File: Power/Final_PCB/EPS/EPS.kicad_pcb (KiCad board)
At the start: 4 copper layers, 85 x 85 mm, 37 parts, among them J1 Left_Header, J2 Right_Header, U1 INA226, U2 MT3608-28, U3 LM2596S-5, U4 LM2596S-3.3

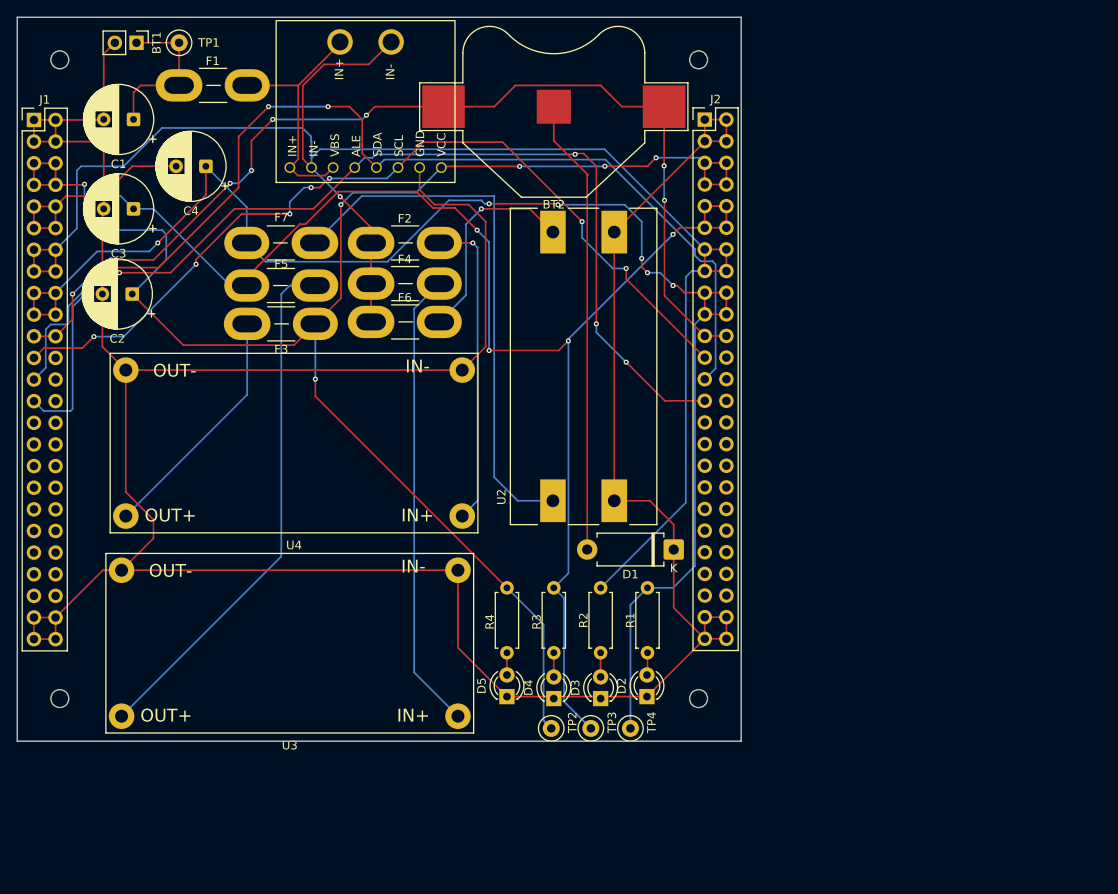
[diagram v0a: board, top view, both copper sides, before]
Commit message: Fixed EPS board to have 12V instead of 28V rail
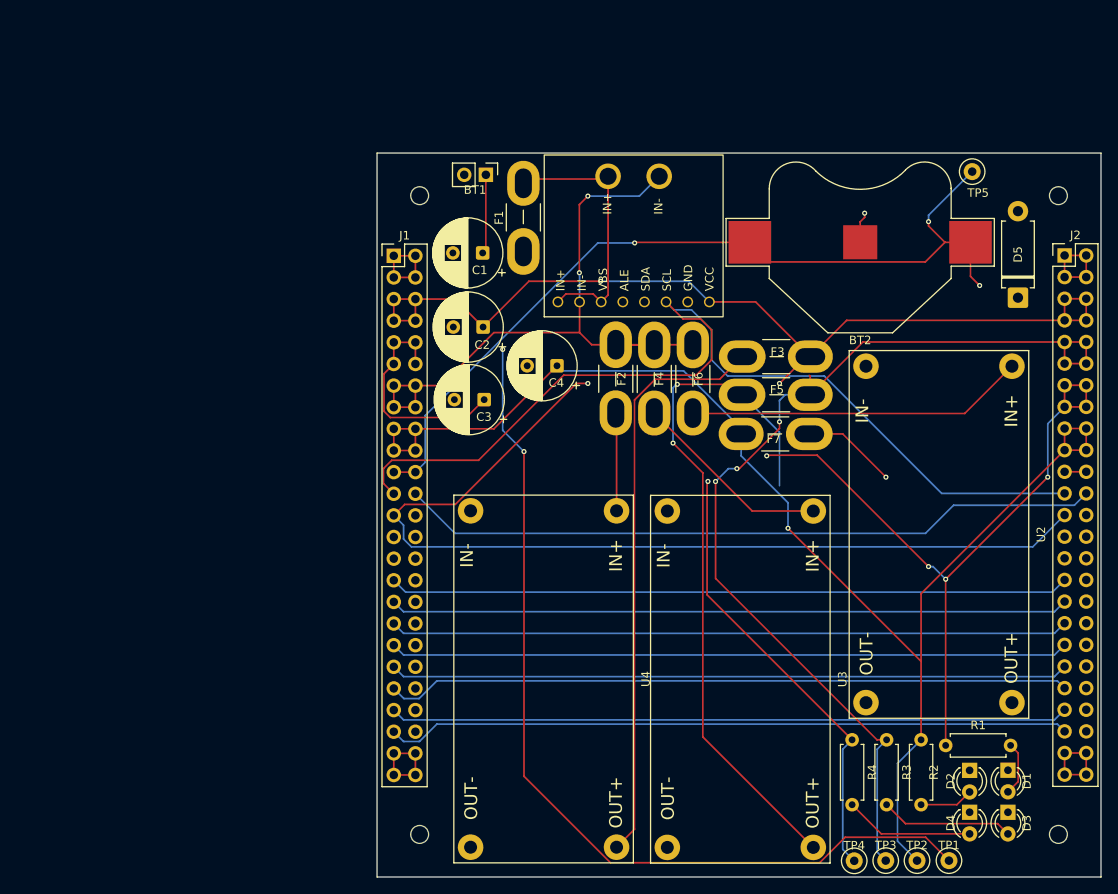
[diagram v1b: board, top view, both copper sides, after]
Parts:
- removed the REF** at (130.0, 124.0)
- removed the REF** at (55.0, 124.0)
- removed the REF** at (130.0, 49.0)
- removed the REF** at (55.0, 49.0)
- added REF**: MountingHole_2.1mm, MountingHole:MountingHole_2.1mm, F.Cu at (172.2, 139.9)
- added REF**: MountingHole_2.1mm, MountingHole:MountingHole_2.1mm, F.Cu at (172.2, 65.0)
- added REF**: MountingHole_2.1mm, MountingHole:MountingHole_2.1mm, F.Cu at (97.2, 139.9)
- added REF**: MountingHole_2.1mm, MountingHole:MountingHole_2.1mm, F.Cu at (97.2, 65.0)
- added TP5: TestPoint, TestPoint:TestPoint_Loop_D2.50mm_Drill1.0mm, F.Cu at (162.1, 62.1)
- D1: value D -> LED; footprint Diode_THT:D_DO-15_P10.16mm_Horizontal -> LED_THT:LED_D3.0mm
- D5: value LED -> D; footprint LED_THT:LED_D3.0mm -> Diode_THT:D_DO-15_P10.16mm_Horizontal
- R1: value 2.7K -> 1.5K
- R2: value 1.5K -> 1K
- R3: value 1K -> 330
- R4: value 330 -> 150
- U2: value MT3608-28 -> LM2596-12; footprint MT3608_Breakout:MODULE_MT3608_DC-DC_STEP_UP_CONVERTER_2A_BOOSTER_MODULE -> LM2596S_Breakout:LM2596_Breakout
- moved TP1 131.9 mm to (159.4, 143.0), turned to -90 degrees
- moved D5 76.1 mm to (167.5, 76.9)
- moved F7 62.2 mm to (143.0, 92.9)
- moved F3 58.3 mm to (135.1, 83.8)
- moved U3 53.1 mm to (134.9, 121.7), turned to -90 degrees
- moved F5 51.8 mm to (135.1, 88.3), turned to 0 degrees
- moved D4 50.6 mm to (161.8, 137.3), turned to -90 degrees
- moved D3 49.7 mm to (166.3, 137.3), turned to -90 degrees
- moved C4 47.4 mm to (113.4, 84.9)
- moved D1 47.0 mm to (166.3, 132.4), turned to -90 degrees
- moved C3 46.9 mm to (104.8, 88.9)
- moved U2 46.2 mm to (158.2, 104.7), turned to -90 degrees
- moved TP2 45.7 mm to (155.7, 143.0), turned to -90 degrees
- moved . 45.2 mm to (135.2, 107.0)
- moved J1 45.2 mm to (94.2, 72.0)
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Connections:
- C4 pad 1: 28V -> 12V
- D1 pad 2: Net-(BT2--) -> Net-(D1-A)
- D5 pad 2: Net-(D5-A) -> Net-(BT2--)
- F7 pad 2: 28V -> 12V
- J1 pad 17: 28V -> 12V
- J1 pad 18: 28V -> 12V
- J1 pad 19: 28V -> 12V
- J1 pad 20: 28V -> 12V
- J1 pad 29: L298N_2_IN4 -> unconnected-(J1-Pin_29-Pad29)
- J1 pad 30: L298N_2_IN3 -> unconnected-(J1-Pin_30-Pad30)
- J2 pad 17: 28V -> 12V
- J2 pad 18: 28V -> 12V
- J2 pad 19: 28V -> 12V
- J2 pad 20: 28V -> 12V
- J2 pad 29: L298N_2_IN4 -> unconnected-(J2-Pin_29-Pad29)
- J2 pad 30: L298N_2_IN3 -> unconnected-(J2-Pin_30-Pad30)
- R1 pad 1: 28V -> 14.8V
- R1 pad 2: Net-(D2-A) -> Net-(D1-A)
- R2 pad 1: 14.8V -> 12V
- R2 pad 2: Net-(D3-A) -> Net-(D2-A)
- R3 pad 2: Net-(D4-A) -> Net-(D3-A)
- R4 pad 2: Net-(D5-A) -> Net-(D4-A)
- TP2 pad 1: 3V3 -> 12V
- TP4 pad 1: 28V -> 3V3
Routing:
- net 28V: track 176.4 -> 0.00 mm, vias 6 -> 0
- net 12V: track 0.00 -> 158.0 mm, vias 0 -> 1
- net Net-(BT1-+): track 19.9 -> 132.8 mm, vias 0 -> 2
- net L298N_2_IN4: track 79.7 -> 0.00 mm
- net L298N_2_IN3: track 79.7 -> 0.00 mm
- net Net-(U4-VOUT+): track 28.5 -> 68.1 mm
- net Net-(BT2--): track 53.7 -> 21.7 mm, vias 0 -> 1
- net Net-(U3-VIN+): track 54.2 -> 23.4 mm
- net Net-(U4-VIN+): track 37.0 -> 11.5 mm, vias 1 -> 0
- net 14.8V: track 202.6 -> 178.1 mm, vias 1 -> 7
- net Net-(U2-VOUT+): track 64.4 -> 43.7 mm, vias 0 -> 1
- net Net-(U3-VOUT+): track 61.7 -> 82.2 mm, vias 0 -> 2
- net Net-(U2-VIN+): track 24.9 -> 39.8 mm, vias 2 -> 0
- net GND: track 359.3 -> 344.5 mm
- net Net-(D3-A): track 2.84 -> 15.7 mm
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
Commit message: Revert EPS schematic and PCB to version with MT3608 boost converter
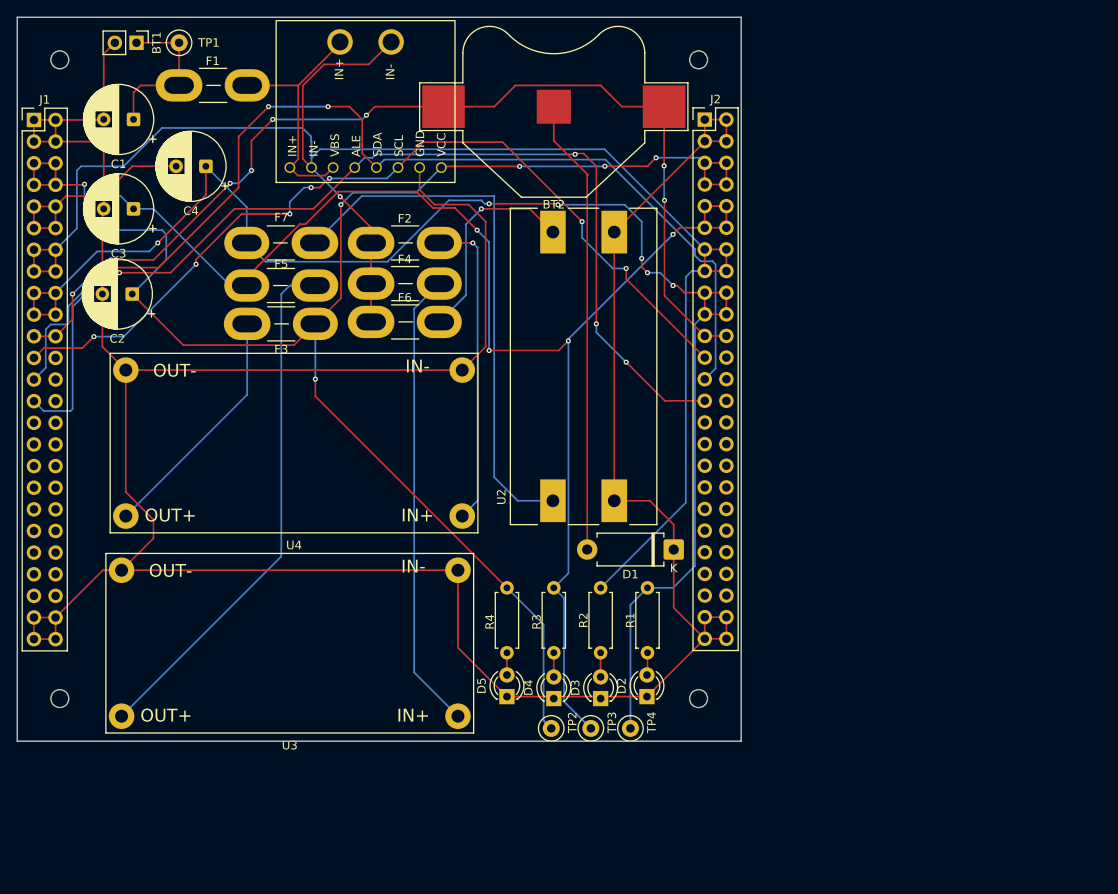
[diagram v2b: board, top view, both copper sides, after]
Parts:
- removed the REF** at (172.2, 139.9)
- removed the REF** at (172.2, 65.0)
- removed the REF** at (97.2, 139.9)
- removed the REF** at (97.2, 65.0)
- removed TP5: TestPoint, TestPoint:TestPoint_Loop_D2.50mm_Drill1.0mm
- added REF**: MountingHole_2.1mm, MountingHole:MountingHole_2.1mm, F.Cu at (130.0, 124.0)
- added REF**: MountingHole_2.1mm, MountingHole:MountingHole_2.1mm, F.Cu at (55.0, 124.0)
- added REF**: MountingHole_2.1mm, MountingHole:MountingHole_2.1mm, F.Cu at (130.0, 49.0)
- added REF**: MountingHole_2.1mm, MountingHole:MountingHole_2.1mm, F.Cu at (55.0, 49.0)
- D1: value LED -> D; footprint LED_THT:LED_D3.0mm -> Diode_THT:D_DO-15_P10.16mm_Horizontal
- D5: value D -> LED; footprint Diode_THT:D_DO-15_P10.16mm_Horizontal -> LED_THT:LED_D3.0mm
- R1: value 1.5K -> 2.7K
- R2: value 1K -> 1.5K
- R3: value 330 -> 1K
- R4: value 150 -> 330
- U2: value LM2596-12 -> MT3608-28; footprint LM2596S_Breakout:LM2596_Breakout -> MT3608_Breakout:MODULE_MT3608_DC-DC_STEP_UP_CONVERTER_2A_BOOSTER_MODULE
- moved TP1 131.9 mm to (69.0, 47.0), turned to 0 degrees
- moved D5 76.1 mm to (107.5, 123.8)
- moved F7 62.2 mm to (85.0, 70.5)
- moved F3 58.3 mm to (77.0, 80.0)
- moved U3 53.1 mm to (82.0, 117.5), turned to 180 degrees
- moved F5 51.8 mm to (85.0, 75.5), turned to 180 degrees
- moved D4 50.6 mm to (113.0, 124.0), turned to 90 degrees
- moved D3 49.7 mm to (118.5, 124.0), turned to 90 degrees
- moved C4 47.4 mm to (72.2, 61.5)
- moved D1 47.0 mm to (127.1, 106.5), turned to 180 degrees
- moved C3 46.9 mm to (63.7, 66.5)
- moved U2 46.2 mm to (116.5, 85.0), turned to 90 degrees
- moved TP2 45.7 mm to (112.7, 127.5), turned to 90 degrees
- moved . 45.2 mm to (93.0, 91.0)
- moved J1 45.2 mm to (52.0, 56.1)
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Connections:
- C4 pad 1: 12V -> 28V
- D1 pad 2: Net-(D1-A) -> Net-(BT2--)
- D5 pad 2: Net-(BT2--) -> Net-(D5-A)
- F7 pad 2: 12V -> 28V
- J1 pad 17: 12V -> 28V
- J1 pad 18: 12V -> 28V
- J1 pad 19: 12V -> 28V
- J1 pad 20: 12V -> 28V
- J1 pad 29: unconnected-(J1-Pin_29-Pad29) -> L298N_2_IN4
- J1 pad 30: unconnected-(J1-Pin_30-Pad30) -> L298N_2_IN3
- J2 pad 17: 12V -> 28V
- J2 pad 18: 12V -> 28V
- J2 pad 19: 12V -> 28V
- J2 pad 20: 12V -> 28V
- J2 pad 29: unconnected-(J2-Pin_29-Pad29) -> L298N_2_IN4
- J2 pad 30: unconnected-(J2-Pin_30-Pad30) -> L298N_2_IN3
- R1 pad 1: 14.8V -> 28V
- R1 pad 2: Net-(D1-A) -> Net-(D2-A)
- R2 pad 1: 12V -> 14.8V
- R2 pad 2: Net-(D2-A) -> Net-(D3-A)
- R3 pad 2: Net-(D3-A) -> Net-(D4-A)
- R4 pad 2: Net-(D4-A) -> Net-(D5-A)
- TP2 pad 1: 12V -> 3V3
- TP4 pad 1: 3V3 -> 28V
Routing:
- net 28V: track 0.00 -> 176.4 mm, vias 0 -> 6
- net 12V: track 158.0 -> 0.00 mm, vias 1 -> 0
- net Net-(BT1-+): track 132.8 -> 19.9 mm, vias 2 -> 0
- net L298N_2_IN4: track 0.00 -> 79.7 mm
- net L298N_2_IN3: track 0.00 -> 79.7 mm
- net Net-(U4-VOUT+): track 68.1 -> 28.5 mm
- net Net-(BT2--): track 21.7 -> 53.7 mm, vias 1 -> 0
- net Net-(U3-VIN+): track 23.4 -> 54.2 mm
- net Net-(U4-VIN+): track 11.5 -> 37.0 mm, vias 0 -> 1
- net 14.8V: track 178.1 -> 202.6 mm, vias 7 -> 1
- net Net-(U2-VOUT+): track 43.7 -> 64.4 mm, vias 1 -> 0
- net Net-(U3-VOUT+): track 82.2 -> 61.7 mm, vias 2 -> 0
- net Net-(U2-VIN+): track 39.8 -> 24.9 mm, vias 0 -> 2
- net GND: track 344.5 -> 359.3 mm
- net Net-(D3-A): track 15.7 -> 2.84 mm
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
